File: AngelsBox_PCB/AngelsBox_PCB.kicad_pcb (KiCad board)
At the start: 2 copper layers, 19 parts

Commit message: Version 1.0 Adds first completed pcb. Adds Gerber files for pcb. Adds 3d stl models for the pcb and first version of keycaps.
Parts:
- MX1, MX10, MX11, MX12, MX13, MX14, MX15, MX2, MX3, MX4, MX5, MX6, MX7, MX8, MX9: footprint AngelBox_Switch_Library:Kailh_Choc-CircleDesign -> AngelBox_Switch_Library:Kailh_Choc_Hotswap-CircleDesign
- MX16, MX17, MX18: footprint Kailh_Choc:KailhChoc-1U -> AngelBox_Switch_Library:KailhChoc-1U-Hotswap
- moved MX14 125.5 mm to (295.0, 53.2)
- moved MX15 124.0 mm to (327.5, 59.2)
- moved MX6 97.8 mm to (248.0, 90.2)
- moved MX8 95.7 mm to (248.0, 123.2)
- moved MX7 95.2 mm to (276.0, 79.7)
- moved MX11 94.0 mm to (305.0, 82.7)
- moved MX9 93.8 mm to (276.0, 112.7)
- moved MX10 93.4 mm to (305.0, 115.7)
- moved MX13 92.7 mm to (331.5, 126.7)
- moved MX12 92.2 mm to (331.5, 93.7)
- moved MX1 88.6 mm to (128.5, 119.2)
- moved MX4 88.0 mm to (211.0, 109.7)
- moved MX2 86.7 mm to (155.0, 101.7)
- moved MX3 86.0 mm to (183.6, 94.2)
- moved MX5 85.4 mm to (224.9, 158.2)
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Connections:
- MX1 pad 2: ROW0 -> GND
- MX10 pad 2: ROW1 -> GND
- MX11 pad 2: ROW1 -> GND
- MX12 pad 2: ROW1 -> GND
- MX13 pad 2: ROW1 -> GND
- MX14 pad 2: ROW1 -> GND
- MX15 pad 2: ROW1 -> GND
- MX16 pad 2: ROW0 -> GND
- MX17 pad 1: COL16 -> COL17
- MX17 pad 2: ROW0 -> GND
- MX18 pad 1: COL17 -> COL16
- MX18 pad 2: ROW0 -> GND
- MX2 pad 2: ROW0 -> GND
- MX3 pad 2: ROW0 -> GND
- MX4 pad 2: ROW0 -> GND
- MX5 pad 2: ROW0 -> GND
- MX6 pad 2: ROW1 -> GND
- MX7 pad 2: ROW1 -> GND
- MX8 pad 2: ROW1 -> GND
- MX9 pad 2: ROW1 -> GND
- U1 pad 0: ROW1 -> COL13
- U1 pad 10: COL5 -> COL3
- U1 pad 12: COL3 -> COL2
- U1 pad 13: COL2 -> COL1
- U1 pad 14: COL1 -> COL0
- U1 pad 15: COL0 -> COL17
- U1 pad 2: COL13 -> COL10
- U1 pad 26: COL17 -> COL16
- U1 pad 27: COL16 -> COL15
- U1 pad 28: COL15 -> unconnected-(U1-GP28-Pad28)
- U1 pad 29: ROW0 -> unconnected-(U1-GP29-Pad29)
- U1 pad 3: COL12 -> COL11
- U1 pad 4: COL11 -> COL12
- U1 pad 5: COL10 -> COL9
- U1 pad 6: COL9 -> COL6
- U1 pad 8: COL7 -> COL5
- U1 pad 9: COL6 -> COL7
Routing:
- net COL12: track 0.00 -> 171.2 mm, vias 0 -> 1
- net COL11: track 0.00 -> 151.2 mm, vias 0 -> 1
- net COL9: track 0.00 -> 135.9 mm, vias 0 -> 1
- net COL14: track 0.00 -> 131.9 mm, vias 0 -> 1
- net COL0: track 0.00 -> 116.5 mm, vias 0 -> 1
- net COL4: track 0.00 -> 113.1 mm, vias 0 -> 1
- net COL10: track 0.00 -> 111.6 mm, vias 0 -> 1
- net COL8: track 0.00 -> 100.4 mm, vias 0 -> 1
- net COL13: track 0.00 -> 89.9 mm, vias 0 -> 1
- net COL7: track 0.00 -> 82.6 mm, vias 0 -> 1
- net COL15: track 0.00 -> 78.7 mm, vias 0 -> 1
- net COL6: track 0.00 -> 75.6 mm, vias 0 -> 1
- net COL1: track 0.00 -> 70.6 mm, vias 0 -> 1
- net COL17: track 0.00 -> 59.7 mm, vias 0 -> 1
- net COL5: track 0.00 -> 56.3 mm, vias 0 -> 1
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- added copper zone on B.Cu, net GND
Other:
- board outline added: 240.1 x 185.4 mm
- board text added: "AngelsBox-v1.0"

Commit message: Adding small updates and a dome key cap
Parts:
- renumbered MX1 to Choc1, MX10 to Choc10, MX11 to Choc11, MX12 to Choc12, MX13 to Choc13, MX14 to Choc14, MX15 to Choc15, MX16 to Choc16, MX17 to Choc17, MX18 to Choc18, MX2 to Choc2, MX3 to Choc3, MX4 to Choc4, MX5 to Choc5, MX6 to Choc6, MX7 to Choc7, MX8 to Choc8, MX9 to Choc9
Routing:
- net COL9: track 135.9 -> 137.4 mm
- net COL8: track 100.4 -> 101.9 mm
- net COL6: track 75.6 -> 77.1 mm
- net COL5: track 56.3 -> 57.8 mm
- net COL14: track 131.9 -> 133.4 mm
- net COL10: track 111.6 -> 113.1 mm
- net COL12: track 171.2 -> 172.7 mm
- net COL11: track 151.2 -> 152.7 mm
- net COL13: track 89.9 -> 91.4 mm
- net COL7: track 82.6 -> 83.3 mm
- net COL3: track 54.8 -> 55.5 mm
- net COL4: track 113.1 -> 113.7 mm
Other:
- outline, holes or cut-outs redrawn

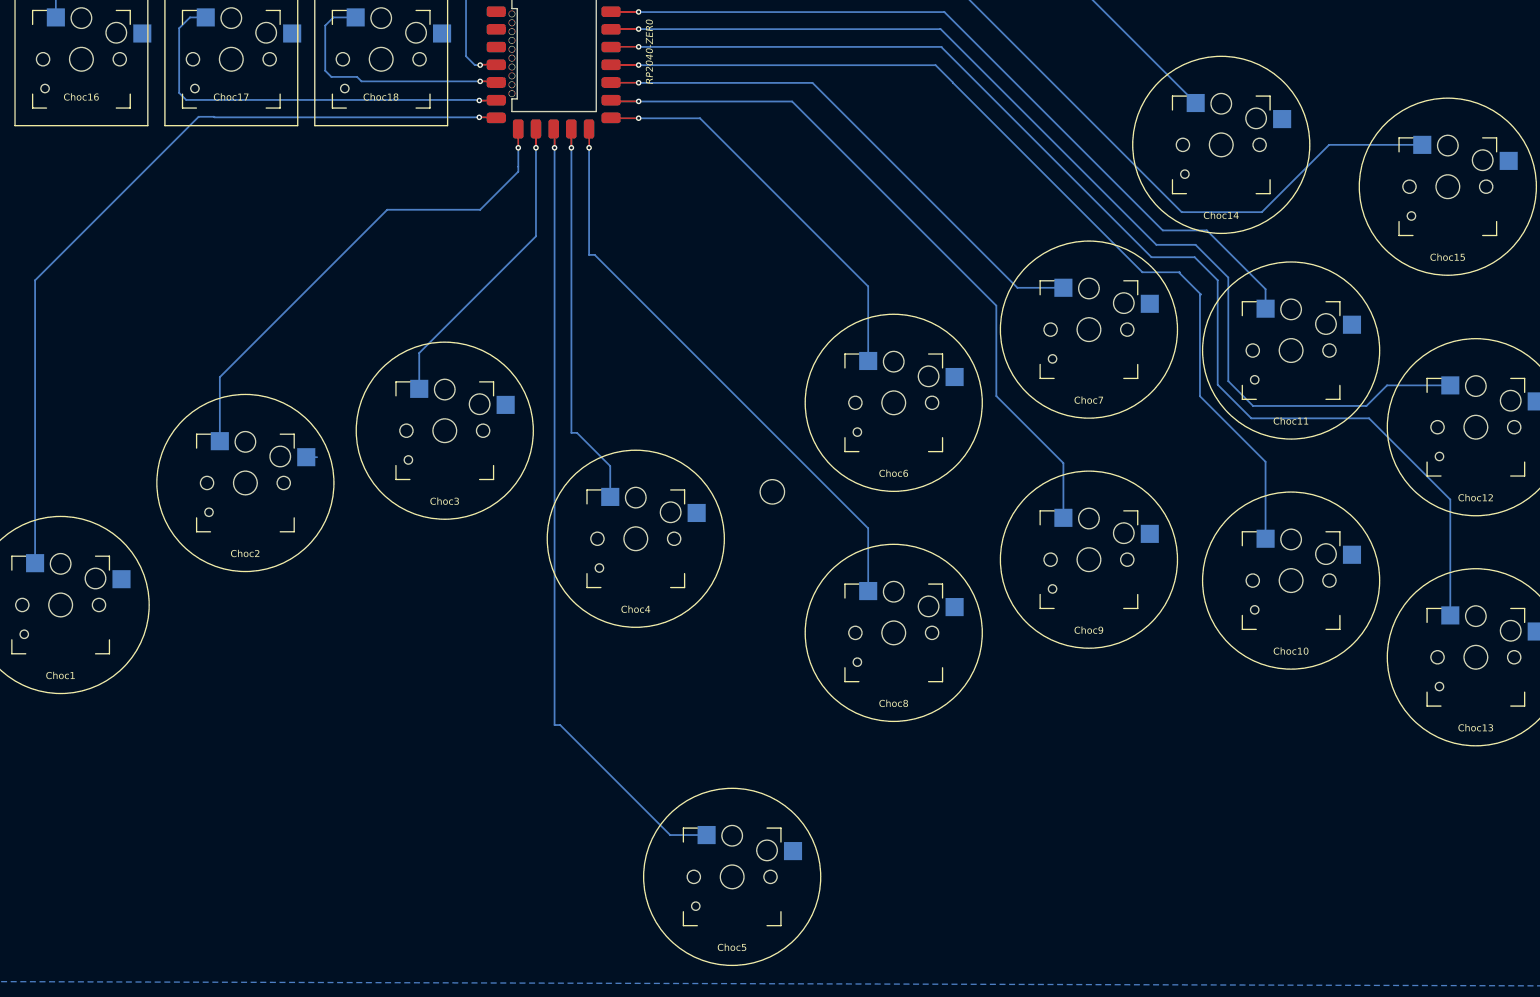
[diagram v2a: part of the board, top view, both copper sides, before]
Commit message: small change to the foot prints for the key switches to support choc v1 and v2
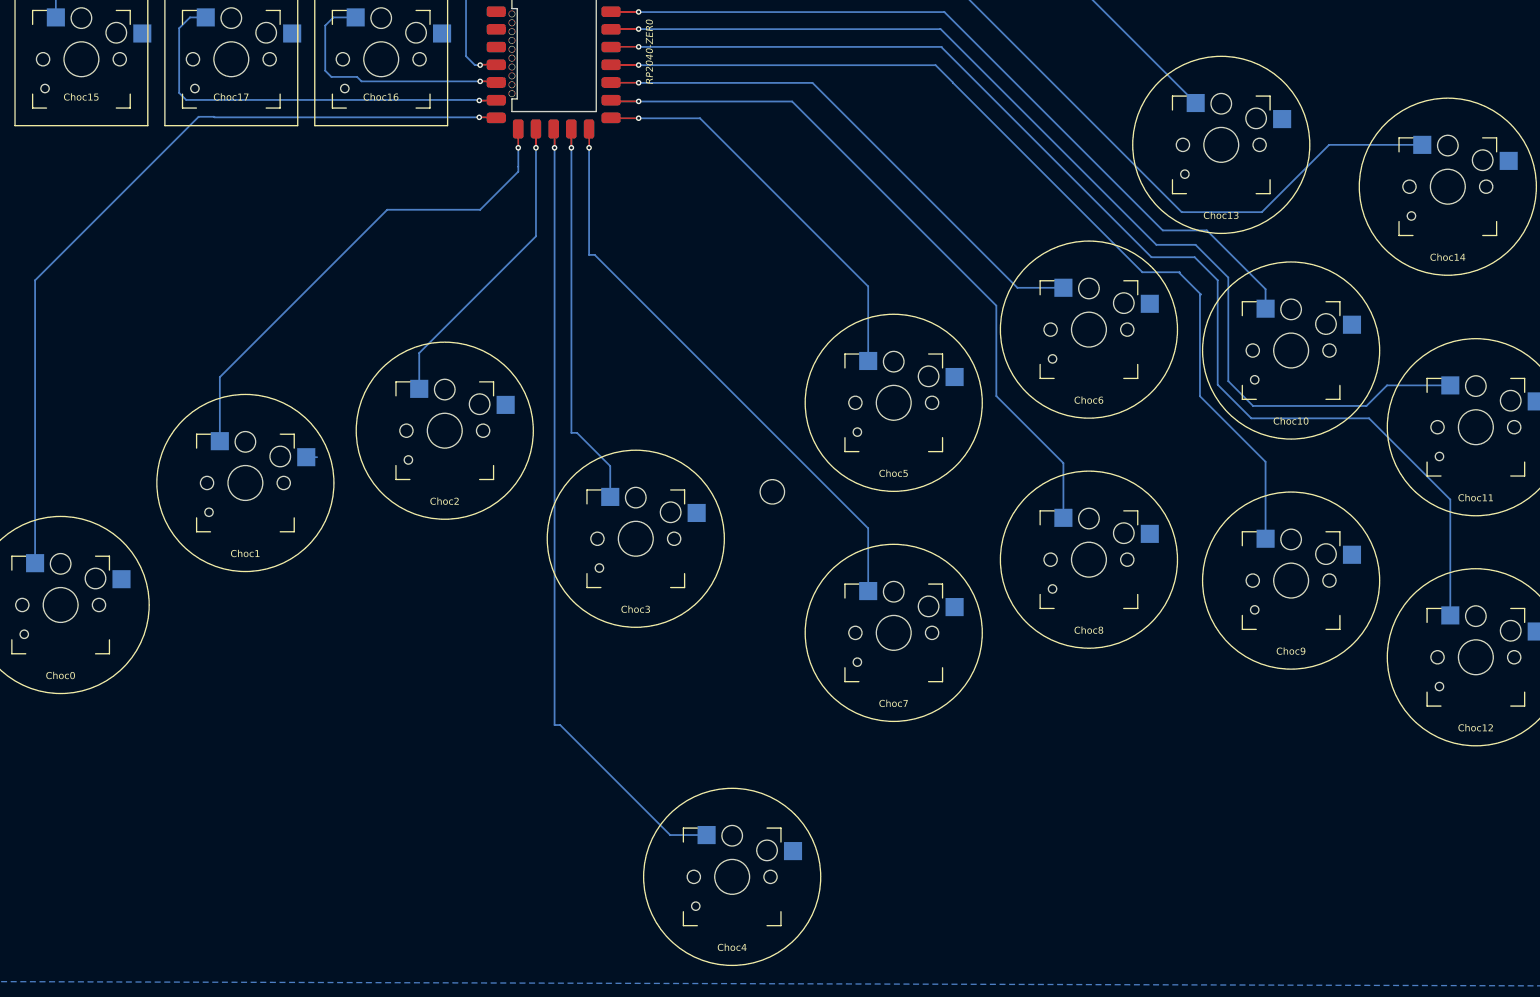
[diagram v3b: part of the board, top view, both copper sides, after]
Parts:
- renumbered Choc1 to Choc0, Choc2 to Choc1, Choc11 to Choc10, Choc12 to Choc11, Choc13 to Choc12, Choc14 to Choc13, Choc15 to Choc14, Choc16 to Choc15, Choc18 to Choc16, Choc3 to Choc2, Choc4 to Choc3, Choc5 to Choc4, Choc6 to Choc5, Choc7 to Choc6, Choc8 to Choc7, Choc9 to Choc8, Choc10 to Choc9
